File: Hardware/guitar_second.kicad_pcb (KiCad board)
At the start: 2 copper layers, 243.8 x 91.5 mm, 63 parts, among them SW1 SW_Push, SW2 SW_Push, SW3 SW_Push, SW4 SW_Push, SW5 SW_Push, U1 PCF8574

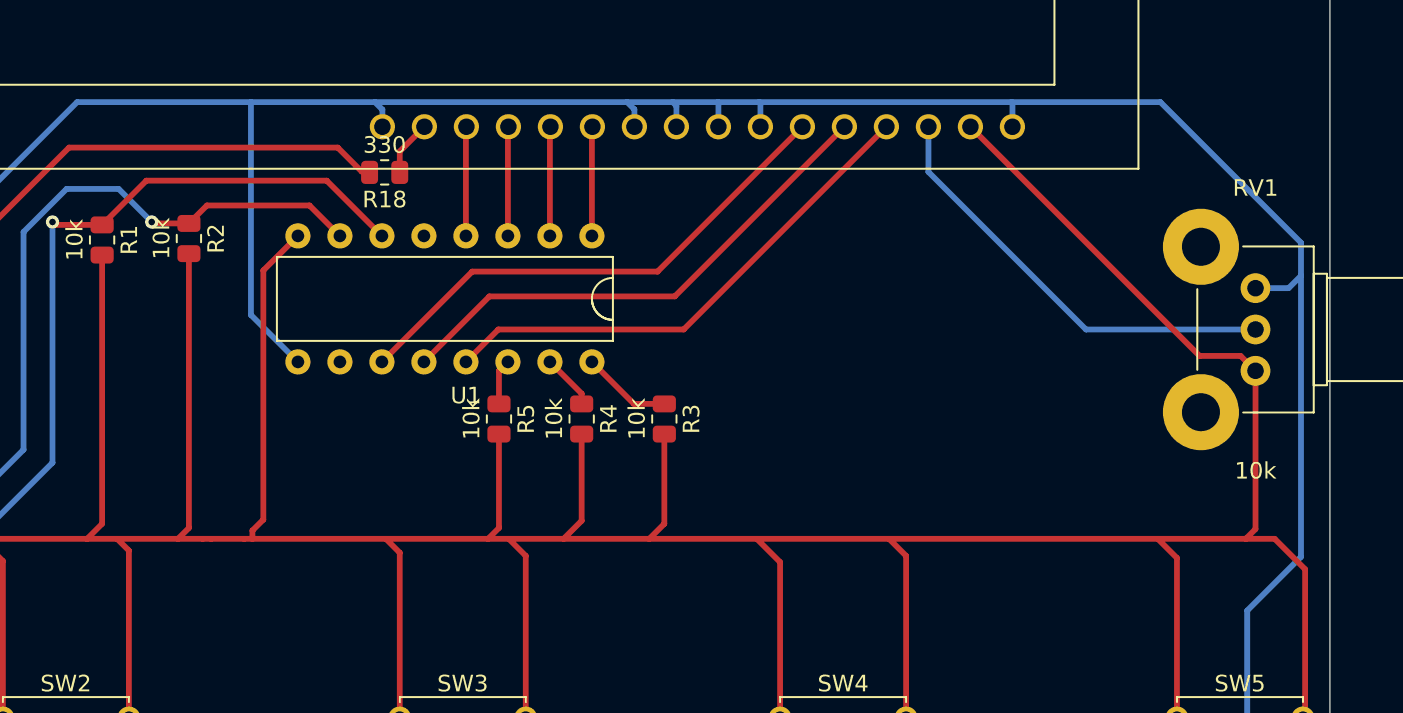
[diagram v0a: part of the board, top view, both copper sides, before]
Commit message: Fixed pin numbering of port expander
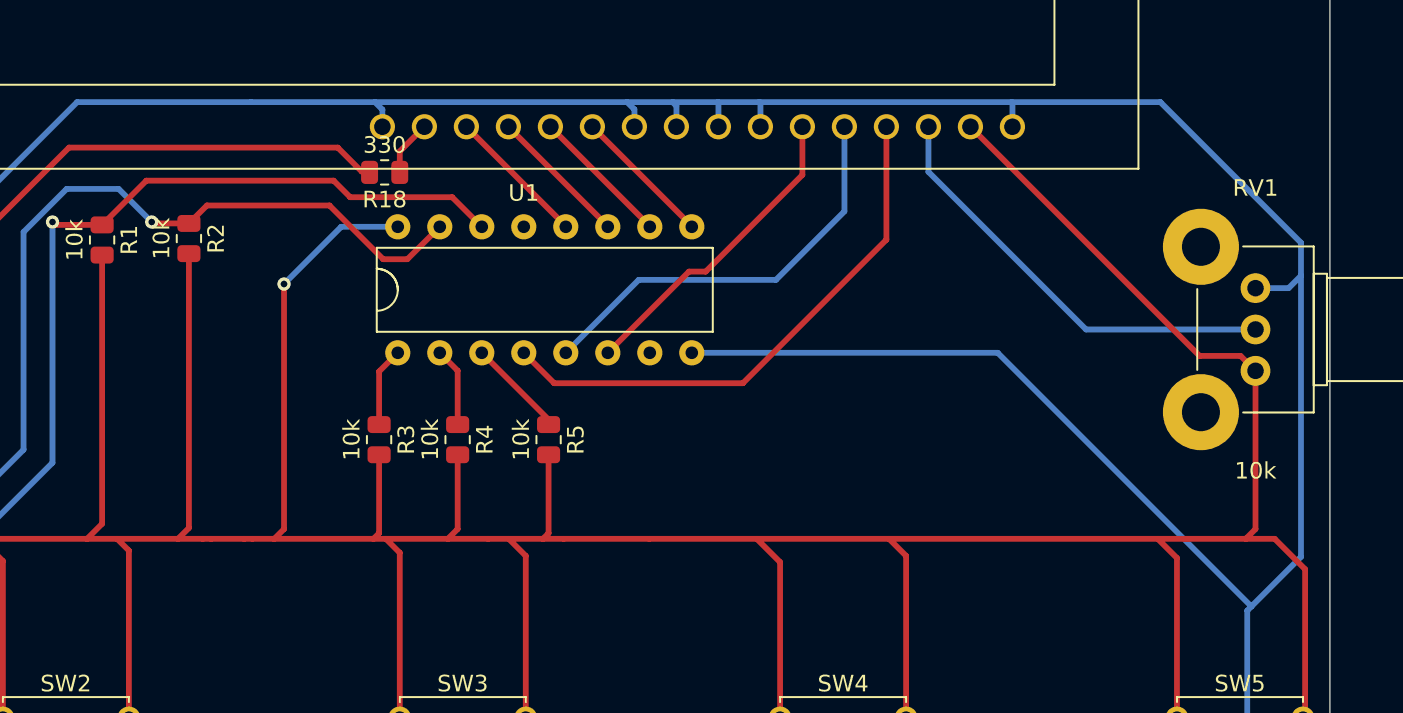
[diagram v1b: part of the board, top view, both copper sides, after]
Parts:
- removed the REF** at (32.2, 134.8) (x2)
- removed the REF** at (32.2, 138.8) (x2)
- removed the REF** at (32.2, 143.8) (x2)
- removed the REF** at (32.2, 147.8) (x2)
- removed the REF** at (32.2, 152.8) (x2)
- removed the REF** at (32.2, 129.8) (x2)
- removed the REF** at (32.2, 125.8) (x2)
- removed the REF** at (32.2, 120.8) (x2)
- removed the REF** at (32.2, 116.8) (x2)
- removed the REF** at (32.2, 111.8) (x2)
- removed the REF** at (32.2, 107.8) (x2)
- removed the REF** at (32.2, 102.8) (x2)
- added REF**: TestPoint_Pad_2.5x2.5mm, TestPoint:TestPoint_Pad_2.5x2.5mm, B.Cu at (32.2, 134.8)
- added REF**: TestPoint_Pad_2.5x2.5mm, TestPoint:TestPoint_Pad_2.5x2.5mm, B.Cu at (32.2, 138.8)
- added REF**: TestPoint_Pad_2.5x2.5mm, TestPoint:TestPoint_Pad_2.5x2.5mm, B.Cu at (32.2, 143.8)
- added REF**: TestPoint_Pad_2.5x2.5mm, TestPoint:TestPoint_Pad_2.5x2.5mm, B.Cu at (32.2, 147.8)
- added REF**: TestPoint_Pad_2.5x2.5mm, TestPoint:TestPoint_Pad_2.5x2.5mm, B.Cu at (32.2, 152.8)
- added REF**: P1, TestPoint:TestPoint_Pad_2.5x2.5mm, F.Cu at (32.2, 152.8)
- added REF**: P2, TestPoint:TestPoint_Pad_2.5x2.5mm, F.Cu at (32.2, 147.8)
- added REF**: P3, TestPoint:TestPoint_Pad_2.5x2.5mm, F.Cu at (32.2, 143.8)
- added REF**: P4, TestPoint:TestPoint_Pad_2.5x2.5mm, F.Cu at (32.2, 138.8)
- added REF**: P5, TestPoint:TestPoint_Pad_2.5x2.5mm, F.Cu at (32.2, 134.8)
- added REF**: P6, TestPoint:TestPoint_Pad_2.5x2.5mm, F.Cu at (32.2, 129.8)
- added REF**: P7, TestPoint:TestPoint_Pad_2.5x2.5mm, F.Cu at (32.2, 125.8)
- added REF**: P8, TestPoint:TestPoint_Pad_2.5x2.5mm, F.Cu at (32.2, 120.8)
- added REF**: P9, TestPoint:TestPoint_Pad_2.5x2.5mm, F.Cu at (32.2, 116.8)
- added REF**: P10, TestPoint:TestPoint_Pad_2.5x2.5mm, F.Cu at (32.2, 111.8)
- added REF**: P11, TestPoint:TestPoint_Pad_2.5x2.5mm, F.Cu at (32.2, 107.8)
- added REF**: P12, TestPoint:TestPoint_Pad_2.5x2.5mm, F.Cu at (32.2, 102.8)
- added REF**: TestPoint_Pad_2.5x2.5mm, TestPoint:TestPoint_Pad_2.5x2.5mm, B.Cu at (32.2, 102.8)
- added REF**: TestPoint_Pad_2.5x2.5mm, TestPoint:TestPoint_Pad_2.5x2.5mm, B.Cu at (32.2, 107.8)
- added REF**: TestPoint_Pad_2.5x2.5mm, TestPoint:TestPoint_Pad_2.5x2.5mm, B.Cu at (32.2, 111.8)
- added REF**: TestPoint_Pad_2.5x2.5mm, TestPoint:TestPoint_Pad_2.5x2.5mm, B.Cu at (32.2, 116.8)
- added REF**: TestPoint_Pad_2.5x2.5mm, TestPoint:TestPoint_Pad_2.5x2.5mm, B.Cu at (32.2, 120.8)
- added REF**: TestPoint_Pad_2.5x2.5mm, TestPoint:TestPoint_Pad_2.5x2.5mm, B.Cu at (32.2, 125.8)
- added REF**: TestPoint_Pad_2.5x2.5mm, TestPoint:TestPoint_Pad_2.5x2.5mm, B.Cu at (32.2, 129.8)
- moved R3 17.3 mm to (217.0, 118.9)
- moved U1 13.7 mm to (225.8, 103.5), turned to 0 degrees
- moved R4 7.60 mm to (221.8, 118.9)
- moved R5 3.25 mm to (227.2, 118.9)
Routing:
- net GND: track 389.5 -> 412.8 mm
- net /LCD_E: track 31.3 -> 19.1 mm
- net /SDA: track 75.4 -> 82.8 mm
- net /SCL: track 79.5 -> 85.3 mm
- net /LCD_RW: track 31.3 -> 25.5 mm
- net Net-(R5-Pad1): track 2.76 -> 6.01 mm
- net /LCD_D6: track 6.61 -> 8.58 mm
- net /LCD_D7: track 6.61 -> 8.58 mm
- net /LCD_D5: track 6.61 -> 8.58 mm
- net /LCD_D4: track 6.61 -> 8.58 mm
- net /LCD_RS: track 31.3 -> 33.1 mm
- net Net-(R4-Pad1): track 3.34 -> 4.79 mm
- net Net-(R3-Pad1): track 5.43 -> 4.81 mm
- net +5V: track 348.1 -> 348.3 mm, vias 0 -> 1
